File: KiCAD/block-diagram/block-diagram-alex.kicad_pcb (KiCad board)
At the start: 4 copper layers, 50.8 x 38.1 mm, 34 parts, among them J1 Conn_01x08, J2 Conn_01x08, J3 Conn_01x10, Q3 NMOS, Q4 NMOS, U1 74LS02, U3 74LS11, U6 LMC555xM

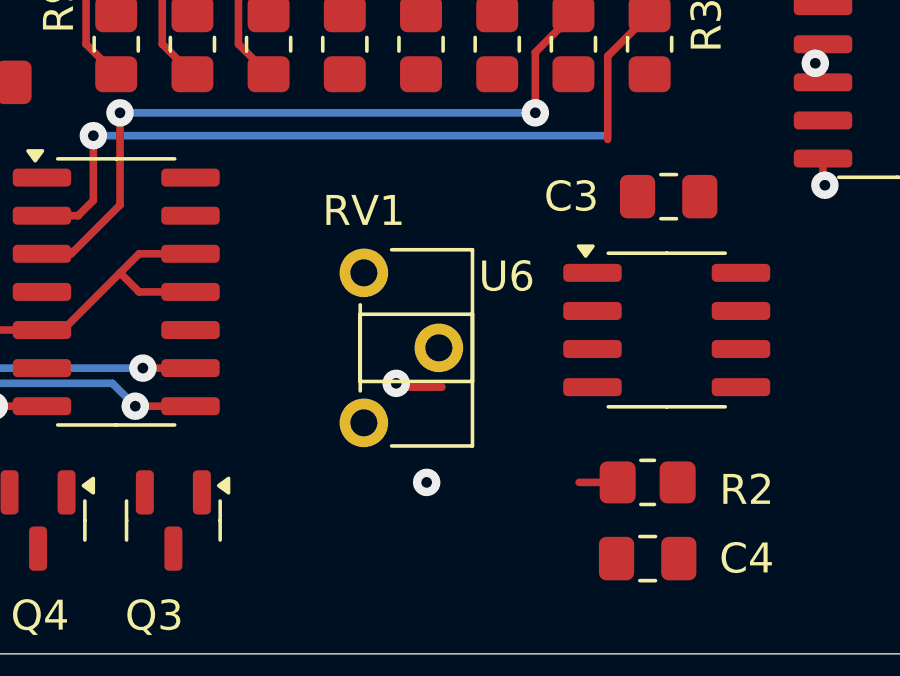
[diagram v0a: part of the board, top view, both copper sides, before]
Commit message: Rotate Pot
Rotated potentiometer so pin 3 is on the left
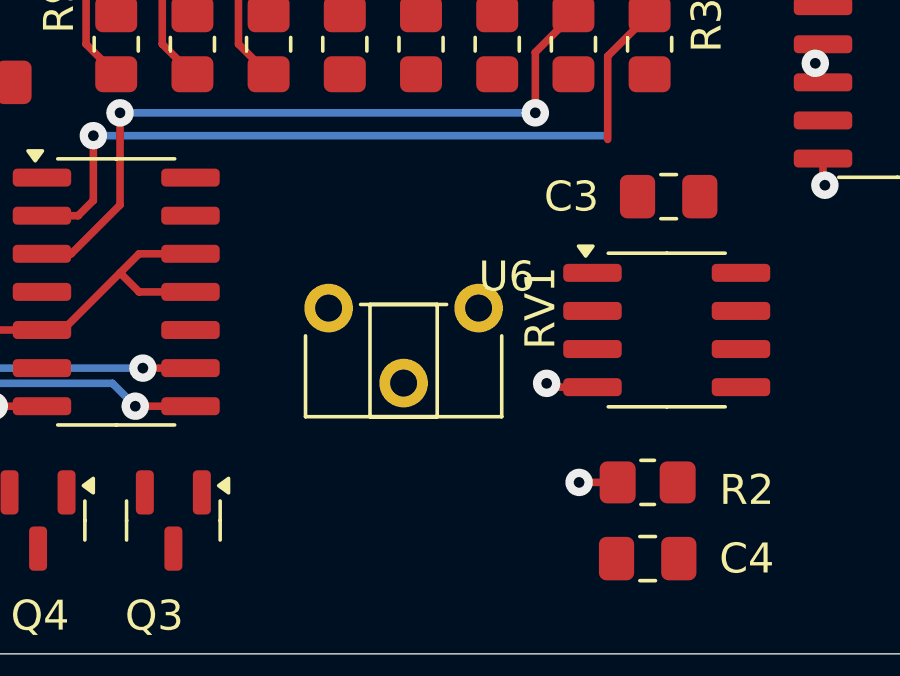
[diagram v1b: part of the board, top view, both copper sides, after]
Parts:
- moved RV1 4.00 mm to (146.1, 97.7), turned to -90 degrees
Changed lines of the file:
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@@
 	(footprint "Potentiometer_THT:Potentiometer_ACP_CA6-H2,5_Horizontal"
 		(layer "F.Cu")
-		(at 142.24 96.52)
+		(at 146.065 97.695 -90)
 		(descr "Potentiometer, horizontal, ACP CA6-H2,5, http://www.acptechnologies.com/wp-content/uploads/2017/06/01-ACP-CA6.pdf")
 		(tags "Potentiometer horizontal ACP CA6-H2,5")
 		(property "Reference" "RV1"
-			(at 0 -2.06 0)
+			(at 0 -2.06 90)
 			(layer "F.SilkS")
 			(effects
@@
 		)
 		(property "Value" "R_Potentiometer_US"
-			(at 0 7.06 0)
+			(at 0 7.06 90)
 			(layer "F.Fab")
 			(effects
@@
 		)
 		(property "Footprint" "Potentiometer_THT:Potentiometer_ACP_CA6-H2,5_Horizontal"
-			(at 0 0 0)
+			(at 0 0 -90)
 			(unlocked yes)
 			(layer "F.Fab")
@@
 		)
 		(property "Datasheet" ""
-			(at 0 0 0)
+			(at 0 0 -90)
 			(unlocked yes)
 			(layer "F.Fab")
@@
 		)
 		(property "Description" "Potentiometer, US symbol"
-			(at 0 0 0)
+			(at 0 0 -90)
 			(unlocked yes)
 			(layer "F.Fab")
@@
 		(attr through_hole)
 		(fp_line
+			(start 0.925 5.77)
+			(end 3.62 5.77)
+			(stroke
+				(width 0.12)
+				(type solid)
+			)
+			(layer "F.SilkS")
+		)
+		(fp_line
+			(start -0.121 3.62)
+			(end 3.62 3.62)
+			(stroke
+				(width 0.12)
+				(type solid)
+			)
+			(layer "F.SilkS")
+		)
+		(fp_line
+			(start -0.121 1.38)
+			(end -0.121 3.62)
+			(stroke
+				(width 0.12)
+				(type solid)
+			)
+			(layer "F.SilkS")
+		)
+		(fp_line
+			(start -0.121 1.38)
+			(end 3.62 1.38)
+			(stroke
+				(width 0.12)
+				(type solid)
+			)
+			(layer "F.SilkS")
+		)
+		(fp_line
+			(start 3.62 1.38)
+			(end 3.62 3.62)
+			(stroke
+				(width 0.12)
+				(type solid)
+			)
+			(layer "F.SilkS")
+		)
+		(fp_line
 			(start -0.121 1.066)
 			(end -0.121 3.935)
@@
 		)
 		(fp_line
-			(start -0.121 1.38)
-			(end -0.121 3.62)
-			(stroke
-				(width 0.12)
-				(type solid)
-			)
-			(layer "F.SilkS")
-		)
-		(fp_line
-			(start -0.121 1.38)
-			(end 3.62 1.38)
-			(stroke
-				(width 0.12)
-				(type solid)
-			)
-			(layer "F.SilkS")
-		)
-		(fp_line
-			(start -0.121 3.62)
-			(end 3.62 3.62)
-			(stroke
-				(width 0.12)
-				(type solid)
-			)
-			(layer "F.SilkS")
-		)
-		(fp_line
 			(start 0.925 -0.77)
 			(end 3.62 -0.77)
@@
 		)
 		(fp_line
-			(start 0.925 5.77)
-			(end 3.62 5.77)
-			(stroke
-				(width 0.12)
-				(type solid)
-			)
-			(layer "F.SilkS")
-		)
-		(fp_line
 			(start 3.62 -0.77)
 			(end 3.62 5.77)
@@
 		)
 		(fp_line
-			(start 3.62 1.38)
-			(end 3.62 3.62)
-			(stroke
-				(width 0.12)
-				(type solid)
-			)
-			(layer "F.SilkS")
+			(start -1.1 6.1)
+			(end 3.75 6.1)
+			(stroke
+				(width 0.05)
+				(type solid)
+			)
+			(layer "F.CrtYd")
+		)
+		(fp_line
+			(start 3.75 6.1)
+			(end 3.75 -1.1)
+			(stroke
+				(width 0.05)
+				(type solid)
+			)
+			(layer "F.CrtYd")
 		)
 		(fp_line
@@
 		)
 		(fp_line
-			(start -1.1 6.1)
-			(end 3.75 6.1)
-			(stroke
-				(width 0.05)
-				(type solid)
-			)
-			(layer "F.CrtYd")
-		)
-		(fp_line
 			(start 3.75 -1.1)
 			(end -1.1 -1.1)
@@
 		)
 		(fp_line
-			(start 3.75 6.1)
-			(end 3.75 -1.1)
-			(stroke
-				(width 0.05)
-				(type solid)
-			)
-			(layer "F.CrtYd")
+			(start 0 5.65)
+			(end 0 -0.65)
+			(stroke
+				(width 0.1)
+				(type solid)
+			)
+			(layer "F.Fab")
+		)
+		(fp_line
+			(start 3.5 5.65)
+			(end 0 5.65)
+			(stroke
+				(width 0.1)
+				(type solid)
+			)
+			(layer "F.Fab")
+		)
+		(fp_line
+			(start 0 3.5)
+			(end 3.5 3.5)
+			(stroke
+				(width 0.1)
+				(type solid)
+			)
+			(layer "F.Fab")
+		)
+		(fp_line
+			(start 3.5 3.5)
+			(end 3.5 1.5)
+			(stroke
+				(width 0.1)
+				(type solid)
+			)
+			(layer "F.Fab")
+		)
+		(fp_line
+			(start 0 1.5)
+			(end 0 3.5)
+			(stroke
+				(width 0.1)
+				(type solid)
+			)
+			(layer "F.Fab")
+		)
+		(fp_line
+			(start 3.5 1.5)
+			(end 0 1.5)
+			(stroke
+				(width 0.1)
+				(type solid)
+			)
+			(layer "F.Fab")
 		)
 		(fp_line
@@
 		)
 		(fp_line
-			(start 0 1.5)
-			(end 0 3.5)
-			(stroke
-				(width 0.1)
-				(type solid)
-			)
-			(layer "F.Fab")
-		)
-		(fp_line
-			(start 0 3.5)
-			(end 3.5 3.5)
-			(stroke
-				(width 0.1)
-				(type solid)
-			)
-			(layer "F.Fab")
-		)
-		(fp_line
-			(start 0 5.65)
-			(end 0 -0.65)
-			(stroke
-				(width 0.1)
-				(type solid)
-			)
-			(layer "F.Fab")
-		)
-		(fp_line
 			(start 3.5 -0.65)
 			(end 3.5 5.65)
@@
 			(layer "F.Fab")
 		)
-		(fp_line
-			(start 3.5 1.5)
-			(end 0 1.5)
-			(stroke
-				(width 0.1)
-				(type solid)
-			)
-			(layer "F.Fab")
-		)
-		(fp_line
-			(start 3.5 3.5)
-			(end 3.5 1.5)
-			(stroke
-				(width 0.1)
-				(type solid)
-			)
-			(layer "F.Fab")
-		)
-		(fp_line
-			(start 3.5 5.65)
-			(end 0 5.65)
-			(stroke
-				(width 0.1)
-				(type solid)
-			)
-			(layer "F.Fab")
-		)
 		(fp_text user "${REFERENCE}"
-			(at 3.59 2.5 0)
+			(at 3.59 2.5 90)
 			(layer "F.Fab")
 			(effects
@@
 		)
 		(pad "1" thru_hole circle
-			(at 0 0)
+			(at 0 0 270)
 			(size 1.62 1.62)
 			(drill 0.9)
@@
 		)
 		(pad "2" thru_hole circle
-			(at 2.5 2.5)
+			(at 2.5 2.5 270)
 			(size 1.62 1.62)
 			(drill 0.9)
@@
 		)
 		(pad "3" thru_hole circle
-			(at 0 5)
+			(at 0 5 270)
 			(size 1.62 1.62)
 			(drill 0.9)
@@
 	)
 	(segment
-		(start 144.845 100.33)
-		(end 143.445 100.33)
+		(start 149.86 100.33)
+		(end 148.46 100.33)
 		(width 0.254)
 		(layer "F.Cu")
 		(net 2)
 	)
-	(segment
-		(start 143.445 100.33)
-		(end 143.318 100.203)
-		(width 0.254)
-		(layer "F.Cu")
-		(net 2)
-	)
 	(via
-		(at 143.318 100.203)
+		(at 148.333 100.203)
 		(size 0.9144)
 		(drill 0.3556)
@@
 	)
 	(via
-		(at 144.334 103.505)
+		(at 149.414 103.505)
 		(size 0.9144)
 		(drill 0.3556)

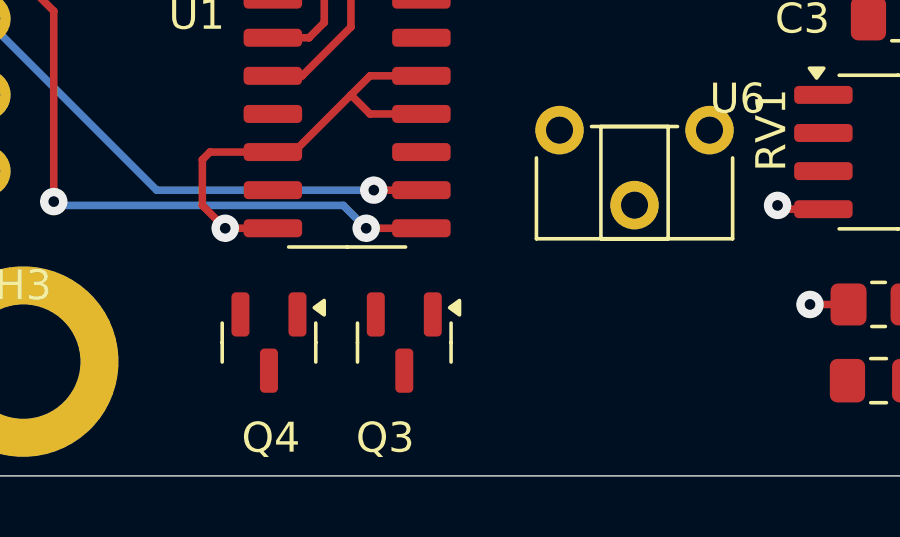
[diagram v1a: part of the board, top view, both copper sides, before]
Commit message: Added some ground vias
Starting to work on routing
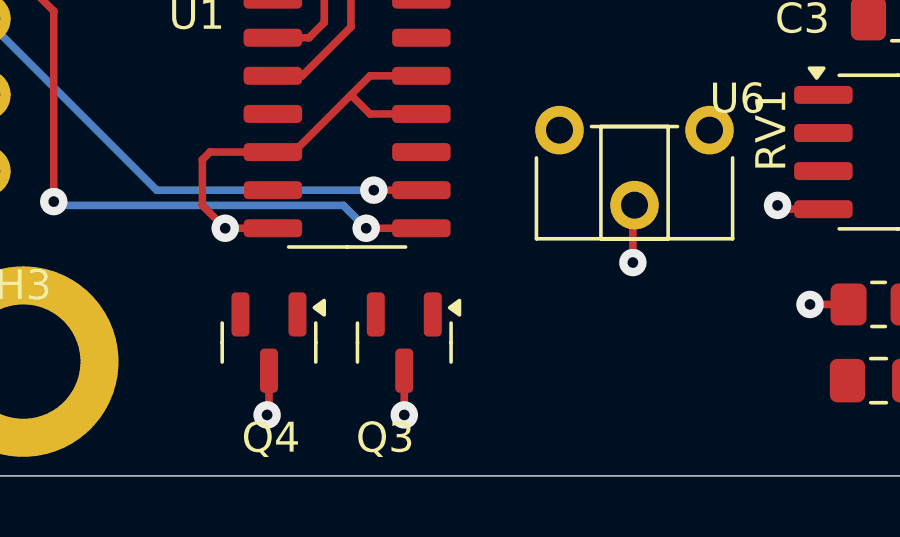
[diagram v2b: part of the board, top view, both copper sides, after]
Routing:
- net GND: track 21.4 -> 26.3 mm, vias 7 -> 10
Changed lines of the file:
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@@
+	)
+	(segment
+		(start 143.565 100.275)
+		(end 143.51 100.33)
+		(width 0.254)
+		(layer "F.Cu")
+		(net 1)
 	)
 	(segment
@@
 	)
 	(segment
+		(start 143.565 100.195)
+		(end 143.565 100.275)
+		(width 0.254)
+		(layer "F.Cu")
+		(net 1)
+	)
+	(segment
 		(start 131.51 98.425)
 		(end 132.207 98.425)
@@
 	)
 	(segment
+		(start 131.38 107.126)
+		(end 131.318 107.188)
+		(width 0.254)
+		(layer "F.Cu")
+		(net 1)
+	)
+	(segment
 		(start 152.917 83.43)
 		(end 153.035 83.312)
@@
 	)
 	(segment
+		(start 143.51 100.33)
+		(end 143.51 102.108)
+		(width 0.254)
+		(layer "F.Cu")
+		(net 1)
+	)
+	(segment
+		(start 131.38 105.7125)
+		(end 131.38 107.126)
+		(width 0.254)
+		(layer "F.Cu")
+		(net 1)
+	)
+	(segment
 		(start 129.159 98.679)
 		(end 129.159 100.203)
@@
 		(net 1)
 	)
+	(segment
+		(start 135.89 105.7125)
+		(end 135.89 107.188)
+		(width 0.254)
+		(layer "F.Cu")
+		(net 1)
+	)
 	(via
 		(at 133.985 82.296)
@@
 	)
 	(via
+		(at 131.318 107.188)
+		(size 0.9144)
+		(drill 0.3556)
+		(layers "F.Cu" "B.Cu")
+		(free yes)
+		(net 1)
+	)
+	(via
+		(at 143.51 102.108)
+		(size 0.9144)
+		(drill 0.3556)
+		(layers "F.Cu" "B.Cu")
+		(free yes)
+		(net 1)
+	)
+	(via
 		(at 153.035 83.312)
 		(size 0.9144)
@@
 		(net 1)
 	)
+	(via
+		(at 135.89 107.188)
+		(size 0.9144)
+		(drill 0.3556)
+		(layers "F.Cu" "B.Cu")
+		(free yes)
+		(net 1)
+	)

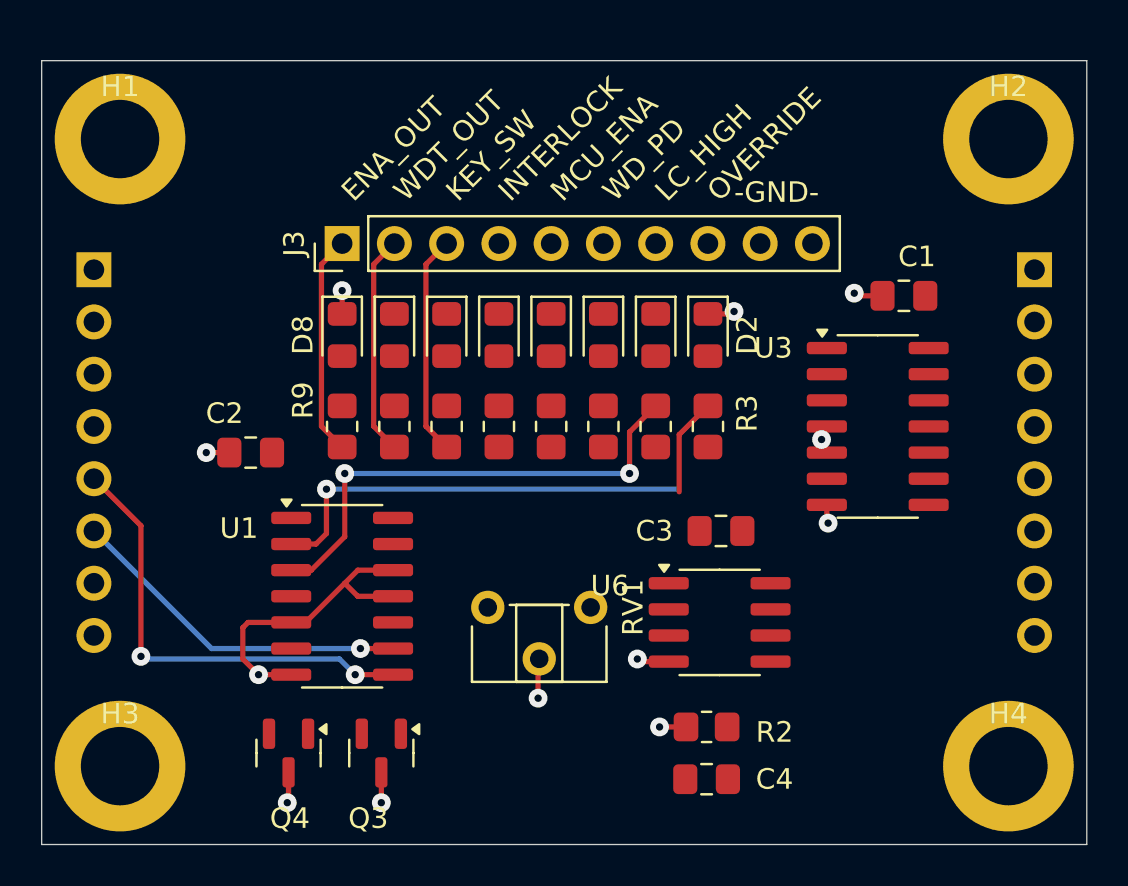
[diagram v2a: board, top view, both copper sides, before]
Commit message: Routing First Attempt
I believe I performed the routing for the board. Note: we should verify which unused pins should be grounded.
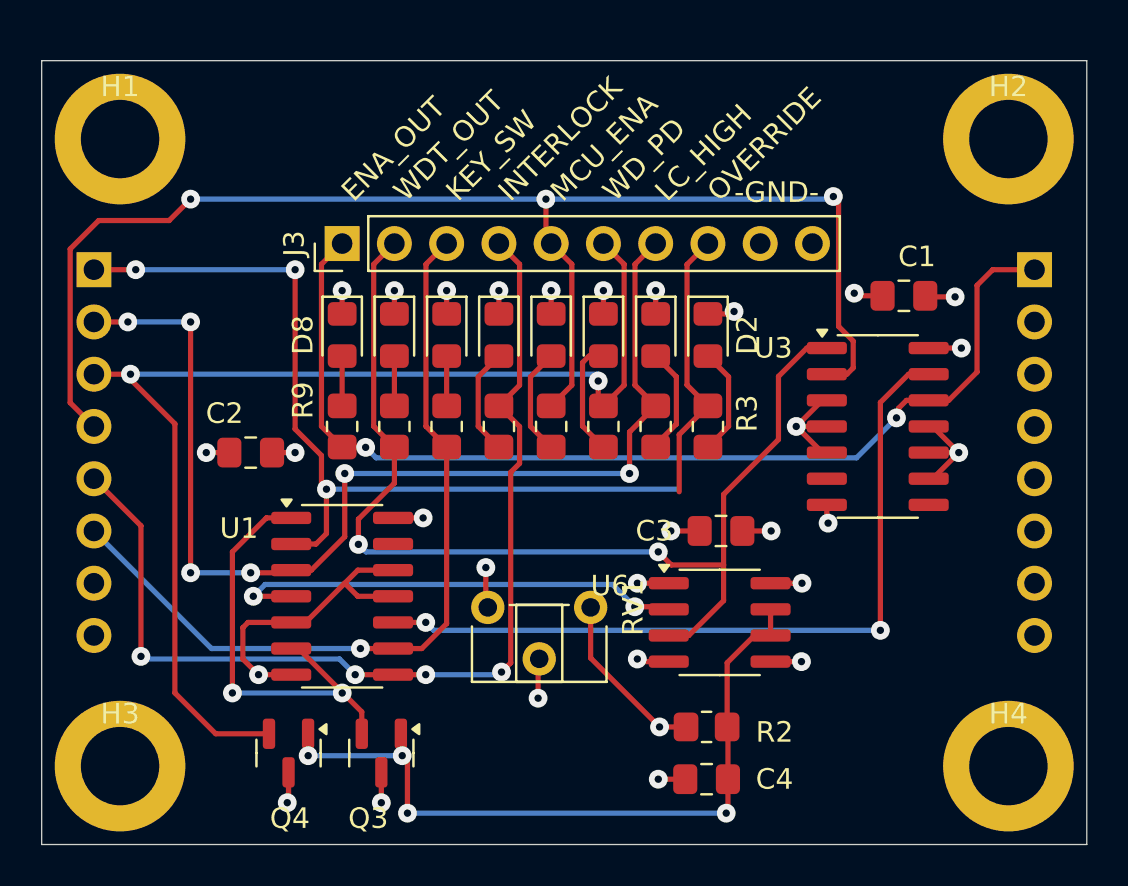
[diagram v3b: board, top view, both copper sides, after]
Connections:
- RV1 pad 1: +5V -> Net-(R2-Pad1)
- RV1 pad 2: GND -> +5V
- RV1 pad 3: Net-(R2-Pad1) -> +5V
- U6 pad 5: unconnected-(U6-CV-Pad5) -> GND
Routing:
- net /MCU_ENA: track 0.00 -> 68.5 mm, vias 0 -> 3
- net /WD_PHOTODIODE: track 0.00 -> 56.6 mm, vias 0 -> 2
- net /WDT_OUT: track 10.7 -> 52.6 mm, vias 0 -> 2
- net /LASER_ENA: track 10.7 -> 51.2 mm, vias 0 -> 2
- net Net-(U1-Pad10): track 0.00 -> 38.0 mm, vias 0 -> 2
- net Net-(Q3-D): track 0.00 -> 36.4 mm, vias 0 -> 4
- net /LC_HIGH: track 24.0 -> 54.6 mm, vias 2 -> 6
- net /OVERRIDE: track 25.9 -> 55.7 mm, vias 1 -> 3
- net /INTERLOCK: track 22.2 -> 50.0 mm, vias 2 -> 4
- net Net-(U6-TR): track 0.00 -> 22.8 mm, vias 0 -> 2
- net GND: track 26.3 -> 48.4 mm, vias 10 -> 20
- net Net-(Q3-G): track 0.00 -> 21.6 mm, vias 0 -> 2
- net +5V: track 1.40 -> 13.9 mm, vias 1 -> 9
- net /KEY_SW: track 27.6 -> 39.3 mm
- net Net-(R2-Pad1): track 1.29 -> 8.48 mm
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
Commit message: Added Via
Fixed weird bug where there was a via that disappeared.
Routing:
- net /OVERRIDE: track 55.7 -> 55.6 mm, vias 3 -> 4
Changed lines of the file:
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@@
-	)
-	(segment
-		(start 150.368 92.075)
-		(end 150.368 89.297)
-		(width 0.254)
-		(layer "F.Cu")
-		(net 24)
 	)
 	(segment
@@
 		(start 131.51 94.615)
 		(end 132.715 94.615)
+		(width 0.254)
+		(layer "F.Cu")
+		(net 24)
+	)
+	(segment
+		(start 150.368 89.297)
+		(end 150.368 91.821)
 		(width 0.254)
 		(layer "F.Cu")
@@
 	)
 	(segment
+		(start 150.368 91.821)
+		(end 150.241 91.948)
+		(width 0.254)
+		(layer "F.Cu")
+		(net 24)
+	)
+	(segment
 		(start 121.92 81.28)
 		(end 123.952 81.28)
@@
 		(size 0.9144)
 		(drill 0.3556)
+		(layers "F.Cu" "B.Cu")
+		(net 24)
+	)
+	(via
+		(at 150.241 91.948)
+		(size 0.9144)
+		(drill 0.3556)

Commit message: Ran DRC
There were only warnings no errors. One useless via was placed, I got rid of it. All other errors referred to the Silkscreen overlapping or being cut off by a component/via. I believe this just refers to the writing printed on the board so I am assuming this is not important.
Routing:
- net Net-(R2-Pad1): vias 1 -> 0
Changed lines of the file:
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@@
-		(net 30)
-	)
-	(via
-		(at 149.414 103.505)
-		(size 0.9144)
-		(drill 0.3556)
-		(layers "F.Cu" "B.Cu")
 		(net 30)
 	)

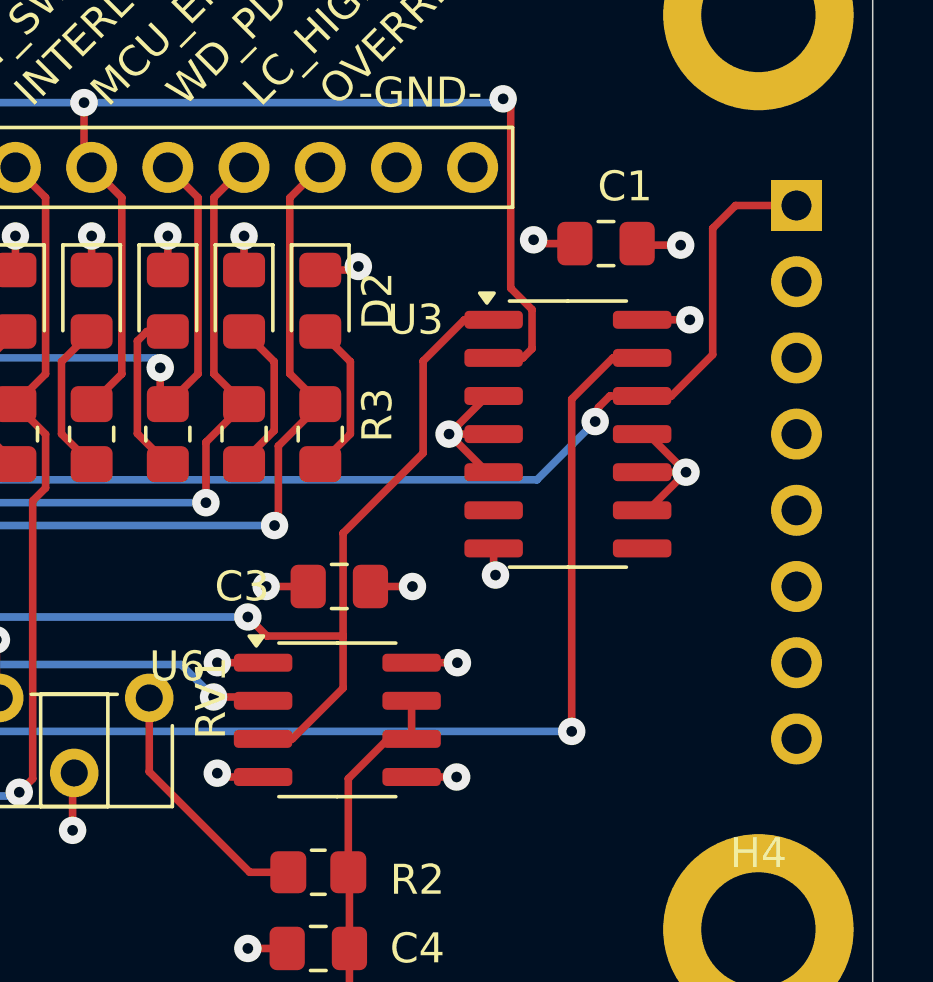
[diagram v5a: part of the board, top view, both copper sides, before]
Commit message: Start filling symbol attributes; move J2 a bit
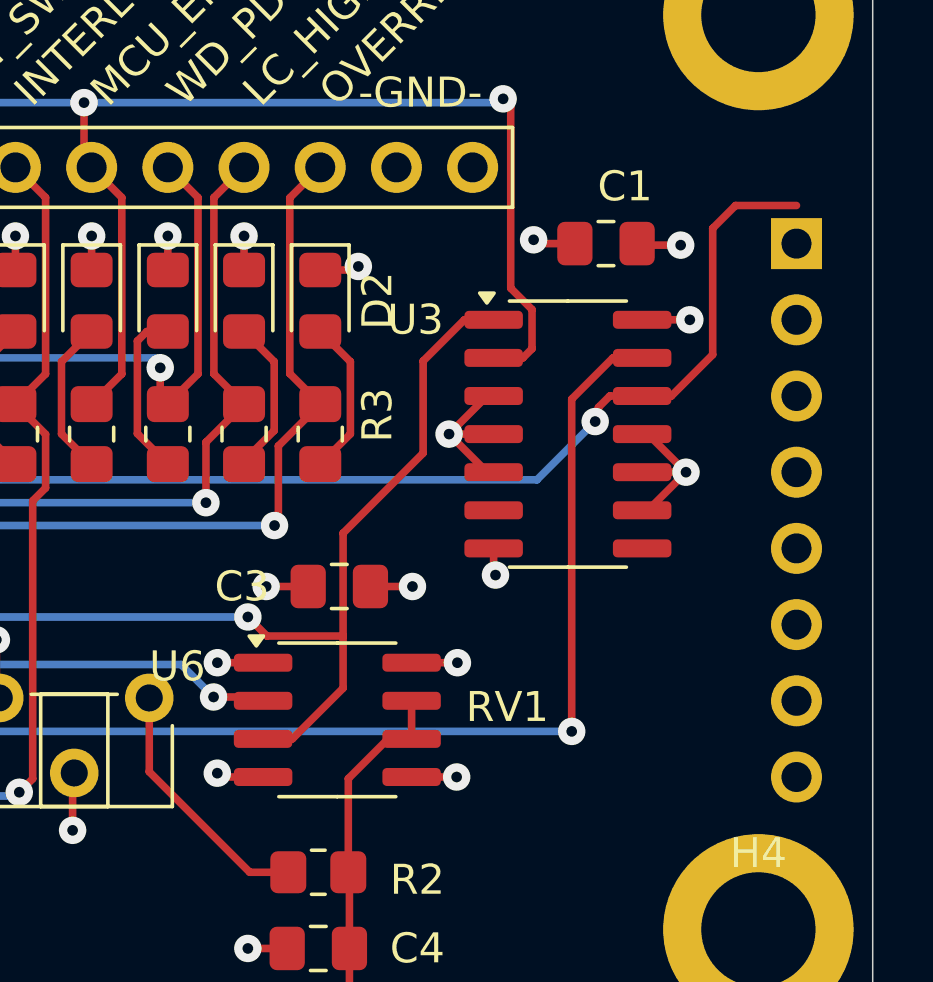
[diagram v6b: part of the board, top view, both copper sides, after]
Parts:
- moved J2 1.27 mm to (167.6, 82.5)
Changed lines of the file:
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@@
 		(tags "Potentiometer horizontal ACP CA6-H2,5")
 		(property "Reference" "RV1"
-			(at 0 -2.06 90)
+			(at 0.305 -11.935 180)
 			(layer "F.SilkS")
 			(effects
@@
 	(footprint "Connector_PinHeader_2.54mm:PinHeader_1x08_P2.54mm_Vertical"
 		(layer "B.Cu")
-		(at 167.64 81.28 180)
+		(at 167.64 82.55 180)
 		(descr "Through hole straight pin header, 1x08, 2.54mm pitch, single row")
 		(tags "Through hole pin header THT 1x08 2.54mm single row")
